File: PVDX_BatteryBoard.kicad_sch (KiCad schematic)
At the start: 2 parts

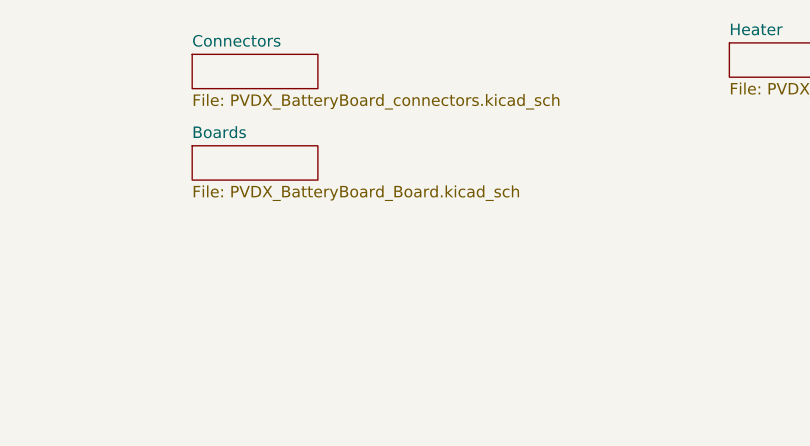
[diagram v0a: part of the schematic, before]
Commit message: Finish battery board schematic (awaiting thermistor part no.)
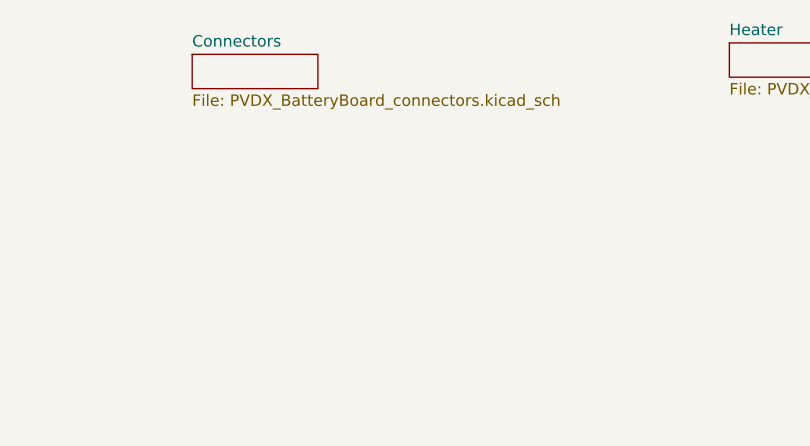
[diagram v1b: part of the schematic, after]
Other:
- removed sheet Boards
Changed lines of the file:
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@@
 (kicad_sch
-	(version 20250114)
+	(version 20260306)
 	(generator "eeschema")
-	(generator_version "9.0")
+	(generator_version "10.0")
 	(paper "A4")
 	(rectangle
@@
 		(at 144.78 106.68 0)
 		(unit 1)
-		(exclude_from_sim no)
-		(in_bom yes)
-		(on_board yes)
+		(body_style 1)
+		(exclude_from_sim no)
+		(in_bom yes)
+		(on_board yes)
+		(in_pos_files yes)
 		(dnp no)
 		(fields_autoplaced yes)
 		(property "Reference" "thermistor_high_temp"
 			(at 147.32 105.4099 0)
+			(show_name no)
+			(do_not_autoplace no)
 			(effects
 				(font
@@
 		(property "Value" "2.498k"
 			(at 147.32 107.9499 0)
+			(show_name no)
+			(do_not_autoplace no)
 			(effects
 				(font
@@
 		(property "Footprint" ""
 			(at 145.796 106.934 90)
-			(effects
-				(font
-					(size 1.27 1.27)
-				)
-				(hide yes)
-			)
-		)
-		(property "Datasheet" "~"
+			(hide yes)
+			(show_name no)
+			(do_not_autoplace no)
+			(effects
+				(font
+					(size 1.27 1.27)
+				)
+			)
+		)
+		(property "Datasheet" ""
 			(at 144.78 106.68 0)
-			(effects
-				(font
-					(size 1.27 1.27)
-				)
-				(hide yes)
+			(hide yes)
+			(show_name no)
+			(do_not_autoplace no)
+			(effects
+				(font
+					(size 1.27 1.27)
+				)
 			)
 		)
 		(property "Description" "Resistor, US symbol"
 			(at 144.78 106.68 0)
-			(effects
-				(font
-					(size 1.27 1.27)
-				)
-				(hide yes)
+			(hide yes)
+			(show_name no)
+			(do_not_autoplace no)
+			(effects
+				(font
+					(size 1.27 1.27)
+				)
 			)
 		)
@@
 		)
 		(instances
-			(project ""
+			(project "PVDX_BatteryBoard"
 				(path "/c318761a-e6d3-4e59-aaa2-0d170bce7cde"
 					(reference "thermistor_high_temp")
@@
 		(at 172.72 107.95 0)
 		(unit 1)
-		(exclude_from_sim no)
-		(in_bom yes)
-		(on_board yes)
+		(body_style 1)
+		(exclude_from_sim no)
+		(in_bom yes)
+		(on_board yes)
+		(in_pos_files yes)
 		(dnp no)
 		(fields_autoplaced yes)
 		(property "Reference" "thermistor_low_temp"
 			(at 175.26 106.6799 0)
+			(show_name no)
+			(do_not_autoplace no)
 			(effects
 				(font
@@
 		(property "Value" "33.476k"
 			(at 175.26 109.2199 0)
+			(show_name no)
+			(do_not_autoplace no)
 			(effects
 				(font
@@
 		(property "Footprint" ""
 			(at 173.736 108.204 90)
-			(effects
-				(font
-					(size 1.27 1.27)
-				)
-				(hide yes)
-			)
-		)
-		(property "Datasheet" "~"
+			(hide yes)
+			(show_name no)
+			(do_not_autoplace no)
+			(effects
+				(font
+					(size 1.27 1.27)
+				)
+			)
+		)
+		(property "Datasheet" ""
 			(at 172.72 107.95 0)
-			(effects
-				(font
-					(size 1.27 1.27)
-				)
-				(hide yes)
+			(hide yes)
+			(show_name no)
+			(do_not_autoplace no)
+			(effects
+				(font
+					(size 1.27 1.27)
+				)
 			)
 		)
 		(property "Description" "Resistor, US symbol"
 			(at 172.72 107.95 0)
-			(effects
-				(font
-					(size 1.27 1.27)
-				)
-				(hide yes)
+			(hide yes)
+			(show_name no)
+			(do_not_autoplace no)
+			(effects
+				(font
+					(size 1.27 1.27)
+				)
 			)
 		)
@@
 		)
 		(instances
-			(project ""
+			(project "PVDX_BatteryBoard"
 				(path "/c318761a-e6d3-4e59-aaa2-0d170bce7cde"
 					(reference "thermistor_low_temp")
@@
 	)
 	(sheet
-		(at 116.84 57.15)
-		(size 13.97 3.81)
+		(at 176.53 45.72)
+		(size 15.24 3.81)
 		(exclude_from_sim no)
 		(in_bom yes)
@@
 		)
 		(fill
-			(color 0 0 0 0.0000)
-		)
-		(property "Sheetname" "Boards"
-			(at 116.84 56.4384 0)
+			(color 0 0 0 0)
+		)
+		(property "Sheetname" "Heater"
+			(at 176.53 45.0084 0)
+			(show_name no)
+			(do_not_autoplace no)
 			(effects
 				(font
@@
 			)
 		)
-		(property "Sheetfile" "PVDX_BatteryBoard_Board.kicad_sch"
-			(at 116.84 61.5446 0)
+		(property "Sheetfile" "PVDX_BatteryBoard_Heater.kicad_sch"
+			(at 176.53 50.1146 0)
+			(show_name no)
+			(do_not_autoplace no)
 			(effects
 				(font
@@
 	)
 	(sheet
-		(at 176.53 45.72)
-		(size 15.24 3.81)
+		(at 116.84 46.99)
+		(size 13.97 3.81)
 		(exclude_from_sim no)
 		(in_bom yes)
@@
 		)
 		(fill
-			(color 0 0 0 0.0000)
-		)
-		(property "Sheetname" "Heater"
-			(at 176.53 45.0084 0)
-			(effects
-				(font
-					(size 1.27 1.27)
-				)
-				(justify left bottom)
-			)
-		)
-		(property "Sheetfile" "PVDX_BatteryBoard_Heater.kicad_sch"
-			(at 176.53 50.1146 0)
-			(effects
-				(font
-					(size 1.27 1.27)
-				)
-				(justify left top)
-			)
-		)
-		(instances
-			(project "PVDX_BatteryBoard"
-				(path "/c318761a-e6d3-4e59-aaa2-0d170bce7cde"
-					(page "4")
-				)
-			)
-		)
-	)
-	(sheet
-		(at 116.84 46.99)
-		(size 13.97 3.81)
-		(exclude_from_sim no)
-		(in_bom yes)
-		(on_board yes)
-		(dnp no)
-		(fields_autoplaced yes)
-		(stroke
-			(width 0.1524)
-			(type solid)
-		)
-		(fill
-			(color 0 0 0 0.0000)
+			(color 0 0 0 0)
 		)
 		(property "Sheetname" "Connectors"
 			(at 116.84 46.2784 0)
+			(show_name no)
+			(do_not_autoplace no)
 			(effects
 				(font
@@
 		(property "Sheetfile" "PVDX_BatteryBoard_connectors.kicad_sch"
 			(at 116.84 51.3846 0)
-			(effects
-				(font
+			(show_name no)
+			(do_not_autoplace no)
+			(effects
+				(font

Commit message: Add thermistor & MOSFET parts/values
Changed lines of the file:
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@@
 	)
 	(sheet
-		(at 176.53 45.72)
+		(at 47.625 58.42)
 		(size 15.24 3.81)
 		(exclude_from_sim no)
@@
 		)
 		(property "Sheetname" "Heater"
-			(at 176.53 45.0084 0)
+			(at 47.625 57.7084 0)
 			(show_name no)
 			(do_not_autoplace no)
@@
 		)
 		(property "Sheetfile" "PVDX_BatteryBoard_Heater.kicad_sch"
-			(at 176.53 50.1146 0)
+			(at 47.625 62.8146 0)
 			(show_name no)
 			(do_not_autoplace no)
@@
 	)
 	(sheet
-		(at 116.84 46.99)
-		(size 13.97 3.81)
+		(at 47.625 47.625)
+		(size 15.24 3.81)
 		(exclude_from_sim no)
 		(in_bom yes)
@@
 		)
 		(property "Sheetname" "Connectors"
-			(at 116.84 46.2784 0)
+			(at 47.625 46.9134 0)
 			(show_name no)
 			(do_not_autoplace no)
@@
 		)
 		(property "Sheetfile" "PVDX_BatteryBoard_connectors.kicad_sch"
-			(at 116.84 51.3846 0)
+			(at 47.625 52.0196 0)
 			(show_name no)
 			(do_not_autoplace no)

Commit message: finished routing
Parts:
- removed thermistor_high_temp: 2.498k, symbol Device:R_US
- removed thermistor_low_temp: 33.476k, symbol Device:R_US
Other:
- note removed: "for reference only"
